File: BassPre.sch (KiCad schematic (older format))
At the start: 38 parts, among them P1 CONN_01X02, P2 CONN_01X02, P3 CONN_01X02, U1 TL072, U2 TL072, U3 TL072

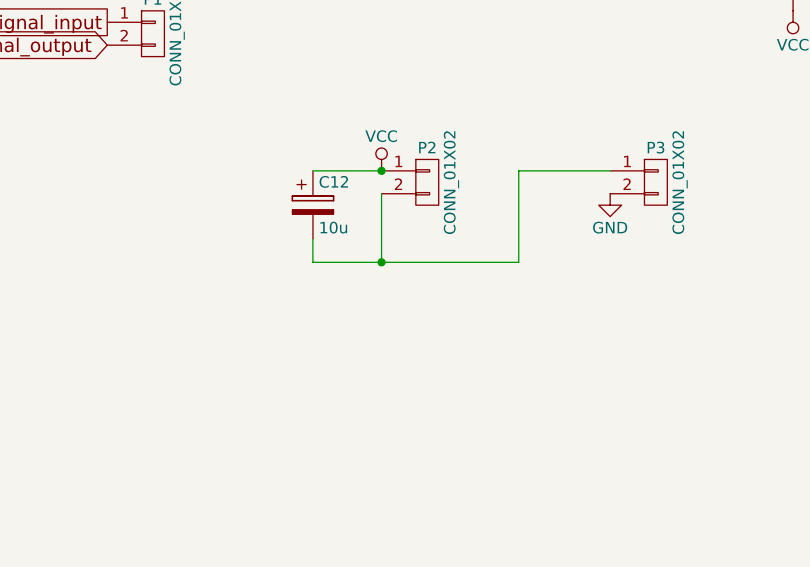
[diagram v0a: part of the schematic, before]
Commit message: fix bypass capacitor position
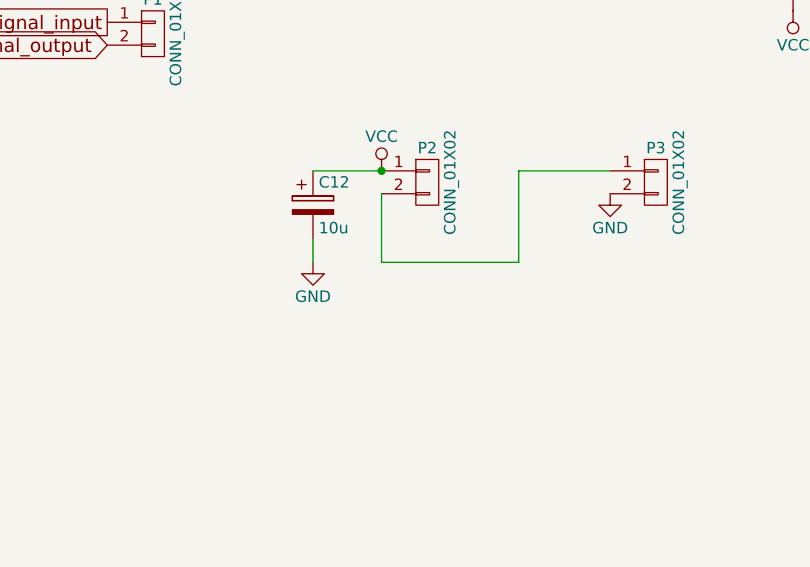
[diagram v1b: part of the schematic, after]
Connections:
- net GND: now also C12.2
- net at P2.2 (P2), P3.1 (P1): no longer C12.2
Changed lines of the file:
@@
 	9300 1600 9300 2000
-Wire Wire Line
-	9300 2000 8400 2000
-Wire Wire Line
-	8700 2000 8700 1700
 Wire Wire Line
 	4100 3300 4100 3750
@@
 Wire Wire Line
 	8400 2000 8400 1900
-Connection ~ 8700 2000
 Wire Wire Line
 	8400 1600 8700 1600
 Connection ~ 8700 1600
+Wire Wire Line
+	9300 2000 8700 2000
+Wire Wire Line
+	8700 2000 8700 1700
+$Comp
+L GND #PWR?
+U 1 1 5A92CE06
+P 8400 2000
+F 0 "#PWR?" H 8400 1750 50  0001 C CNN
+F 1 "GND" H 8400 1850 50  0000 C CNN
+F 2 "" H 8400 2000 50  0000 C CNN
+F 3 "" H 8400 2000 50  0000 C CNN
+	1    8400 2000
+	1    0    0    -1
+$EndComp
 $EndSCHEMATC
